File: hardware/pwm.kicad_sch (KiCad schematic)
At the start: 0 parts

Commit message: block refactoring
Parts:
- added D10: D_SCHOTTKY_30V, Diode_SMD:D_SOD-123, symbol Device:D_Schottky
- added J5: Conn_01x02/PWM, TerminalBlock:TerminalBlock_Altech_AK300-2_P5.00mm, symbol Connector_Generic:Conn_01x02
- added JP1: SolderJumper_3_Bridged12, Jumper:SolderJumper-3_P1.3mm_Bridged12_Pad1.0x1.5mm_NumberLabels, symbol Jumper:SolderJumper_3_Bridged12
- added Q2: AO3400A, Package_TO_SOT_SMD:SOT-23, symbol Transistor_FET:AO3400A
- added R7: 10k, Resistor_SMD:R_0603_1608Metric, symbol Device:R
- added R8: 100, Resistor_SMD:R_0603_1608Metric, symbol Device:R
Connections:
- new net: Q2.1 (G), R8.2
- new net +5V: JP1.1 (A)
- new net GND: Q2.2 (S), R7.1
- new net PWM1: R7.2, R8.1
- new net PWM_NEG: D10.2 (A), J5.1 (Pin_1), Q2.3 (D)
- new net PWM_POS: D10.1 (K), J5.2 (Pin_2), JP1.2 (C)
- new net VIN_PROTECTED: JP1.3 (B)

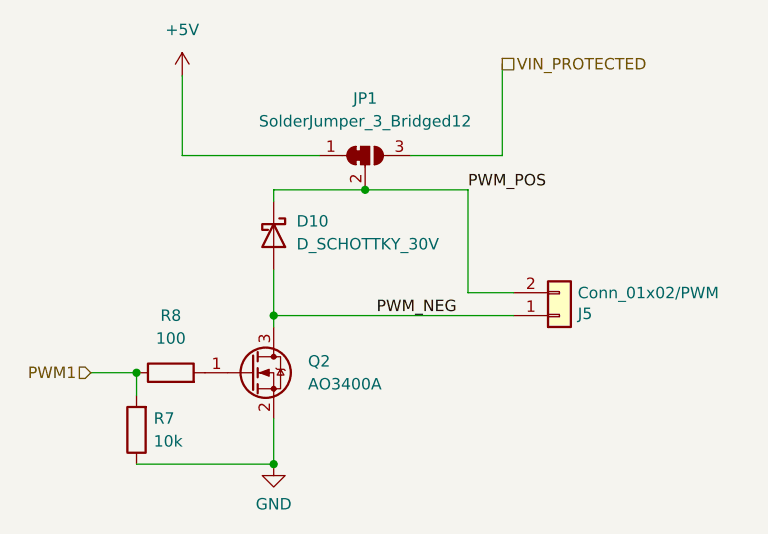
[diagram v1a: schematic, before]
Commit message: Added 3D models and ran freerouting
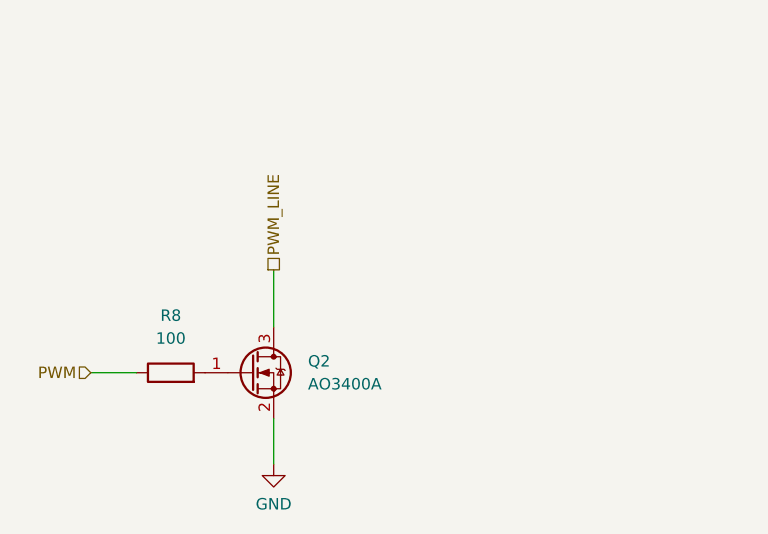
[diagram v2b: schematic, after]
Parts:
- removed D10: D_SCHOTTKY_30V, Diode_SMD:D_SOD-123, symbol Device:D_Schottky
- removed J5: Conn_01x02/PWM, TerminalBlock:TerminalBlock_Altech_AK300-2_P5.00mm, symbol Connector_Generic:Conn_01x02
- removed JP1: SolderJumper_3_Bridged12, Jumper:SolderJumper-3_P1.3mm_Bridged12_Pad1.0x1.5mm_NumberLabels, symbol Jumper:SolderJumper_3_Bridged12
- removed R7: 10k, Resistor_SMD:R_0603_1608Metric, symbol Device:R
- R8: footprint Resistor_SMD:R_0603_1608Metric -> Resistor_SMD:R_0805_2012Metric
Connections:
- net PWM1 renamed PWM
- net PWM_NEG renamed PWM_LINE
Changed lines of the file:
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@@
 (kicad_sch (version 20230121) (generator eeschema)
   (paper "A4")
-  (junction (at 191.77 62.23) (diameter 0) (color 0 0 0 0)
-  )
-  (junction (at 181.61 92.71) (diameter 0) (color 0 0 0 0)
-  )
-  (junction (at 181.61 76.2) (diameter 0) (color 0 0 0 0)
-  )
-  (junction (at 166.37 82.55) (diameter 0) (color 0 0 0 0)
-  )
-  (wire (pts (xy 203.2 73.66) (xy 208.28 73.66))
-    (stroke (width 0) (type default))
-  )
-  (wire (pts (xy 166.37 82.55) (xy 166.37 85.09))
-    (stroke (width 0) (type default))
-  )
-  (wire (pts (xy 181.61 62.23) (xy 181.61 63.5))
-    (stroke (width 0) (type default))
-  )
   (wire (pts (xy 181.61 87.63) (xy 181.61 92.71))
-    (stroke (width 0) (type default))
-  )
-  (wire (pts (xy 181.61 62.23) (xy 191.77 62.23))
-    (stroke (width 0) (type default))
-  )
-  (wire (pts (xy 171.45 49.53) (xy 171.45 58.42))
-    (stroke (width 0) (type default))
-  )
-  (wire (pts (xy 181.61 76.2) (xy 208.28 76.2))
-    (stroke (width 0) (type default))
-  )
-  (wire (pts (xy 191.77 62.23) (xy 203.2 62.23))
     (stroke (width 0) (type default))
   )
@@
     (stroke (width 0) (type default))
   )
-  (wire (pts (xy 181.61 76.2) (xy 181.61 77.47))
+  (wire (pts (xy 181.61 71.12) (xy 181.61 77.47))
     (stroke (width 0) (type default))
   )
-  (wire (pts (xy 166.37 92.71) (xy 181.61 92.71))
-    (stroke (width 0) (type default))
-  )
-  (wire (pts (xy 207.01 58.42) (xy 196.85 58.42))
-    (stroke (width 0) (type default))
-  )
-  (wire (pts (xy 181.61 71.12) (xy 181.61 76.2))
-    (stroke (width 0) (type default))
-  )
-  (wire (pts (xy 171.45 58.42) (xy 186.69 58.42))
-    (stroke (width 0) (type default))
-  )
-  (wire (pts (xy 207.01 48.26) (xy 207.01 58.42))
-    (stroke (width 0) (type default))
-  )
-  (wire (pts (xy 203.2 62.23) (xy 203.2 73.66))
-    (stroke (width 0) (type default))
-  )
-  (label "PWM_NEG" (at 193.04 76.2 0) (fields_autoplaced)
-    (effects (font (size 1.27 1.27)) (justify left bottom))
-  )
-  (label "PWM_POS" (at 203.2 62.23 0) (fields_autoplaced)
-    (effects (font (size 1.27 1.27)) (justify left bottom))
-  )
-  (hierarchical_label "VIN_PROTECTED" (shape passive) (at 207.01 48.26 0) (fields_autoplaced)
-    (effects (font (size 1.27 1.27)) (justify left))
-  )
-  (hierarchical_label "PWM1" (shape input) (at 161.29 82.55 180) (fields_autoplaced)
+  (hierarchical_label "PWM" (shape input) (at 161.29 82.55 180) (fields_autoplaced)
     (effects (font (size 1.27 1.27)) (justify right))
   )
-  (symbol (lib_id "Device:D_Schottky") (at 181.61 67.31 270) (unit 1)
-    (in_bom yes) (on_board yes) (dnp no) (fields_autoplaced)
-    (property "Reference" "D10" (at 184.15 65.7225 90)
-      (effects (font (size 1.27 1.27)) (justify left))
-    )
-    (property "Value" "D_SCHOTTKY_30V" (at 184.15 68.2625 90)
-      (effects (font (size 1.27 1.27)) (justify left))
-    )
-    (property "Footprint" "Diode_SMD:D_SOD-123" (at 181.61 67.31 0)
-      (effects (font (size 1.27 1.27)) hide)
-    )
-    (property "Datasheet" "~" (at 181.61 67.31 0)
-      (effects (font (size 1.27 1.27)) hide)
-    )
-    (property "Cost" "0.0297" (at 181.61 67.31 0)
-      (effects (font (size 1.27 1.27)) hide)
-    )
-    (property "LCSC" "C8598" (at 181.61 67.31 0)
-      (effects (font (size 1.27 1.27)) hide)
-    )
-    (property "Part" "B5819W SL" (at 181.61 67.31 0)
-      (effects (font (size 1.27 1.27)) hide)
-    )
-    (pin "1")
-    (pin "2")
-    (instances
-      (project "esp32-multitool"
-        (path "/3d8a08e7-1222-4d27-bd08-b4e997cf9472/091011c6-be4e-4c21-96a3-2250503f4bfb"
-          (reference "D10") (unit 1)
-        )
-      )
-    )
+  (hierarchical_label "PWM_LINE" (shape passive) (at 181.61 71.12 90) (fields_autoplaced)
+    (effects (font (size 1.27 1.27)) (justify left))
   )
   (symbol (lib_id "Transistor_FET:AO3400A") (at 179.07 82.55 0) (unit 1)
@@
           (reference "Q2") (unit 1)
         )
-      )
-    )
-  )
-  (symbol (lib_id "power:+5V") (at 171.45 49.53 0) (unit 1)
-    (in_bom yes) (on_board yes) (dnp no) (fields_autoplaced)
-    (property "Reference" "#PWR01" (at 171.45 53.34 0)
-      (effects (font (size 1.27 1.27)) hide)
-    )
-    (property "Value" "+5V" (at 171.45 44.45 0)
-      (effects (font (size 1.27 1.27)))
-    )
-    (property "Footprint" "" (at 171.45 49.53 0)
-      (effects (font (size 1.27 1.27)) hide)
-    )
-    (property "Datasheet" "" (at 171.45 49.53 0)
-      (effects (font (size 1.27 1.27)) hide)
-    )
-    (pin "1")
-    (instances
-      (project "esp32-multitool"
-        (path "/3d8a08e7-1222-4d27-bd08-b4e997cf9472/091011c6-be4e-4c21-96a3-2250503f4bfb"
-          (reference "#PWR01") (unit 1)
-        )
-      )
-    )
-  )
-  (symbol (lib_id "Connector_Generic:Conn_01x02") (at 213.36 76.2 0) (mirror x) (unit 1)
-    (in_bom yes) (on_board yes) (dnp no)
-    (property "Reference" "J5" (at 215.392 75.9968 0)
-      (effects (font (size 1.27 1.27)) (justify left))
-    )
-    (property "Value" "Conn_01x02/PWM" (at 215.392 73.6854 0)
-      (effects (font (size 1.27 1.27)) (justify left))
-    )
-    (property "Footprint" "TerminalBlock:TerminalBlock_Altech_AK300-2_P5.00mm" (at 213.36 76.2 0)
-      (effects (font (size 1.27 1.27)) hide)
-    )
-    (property "Datasheet" "~" (at 213.36 76.2 0)
-      (effects (font (size 1.27 1.27)) hide)
-    )
-    (property "LCSC" "C145961" (at 213.36 76.2 0)
-      (effects (font (size 1.27 1.27)) hide)
-    )
-    (property "Cost" "0.0552" (at 213.36 76.2 0)
-      (effects (font (size 1.27 1.27)) hide)
-    )
-    (property "Part" "C145961" (at 213.36 76.2 0)
-      (effects (font (size 1.27 1.27)) hide)
-    )
-    (pin "1")
-    (pin "2")
-    (instances
-      (project "i2c"
-        (path "/2404772b-3ee1-43f3-b842-72bbeb108397"
-          (reference "J5") (unit 1)
-        )
-      )
-      (project "esp32-multitool"
-        (path "/3d8a08e7-1222-4d27-bd08-b4e997cf9472/f9d349b3-837f-44a8-8ae1-0f3a2a1be1fb"
-          (reference "J3") (unit 1)
-        )
-        (path "/3d8a08e7-1222-4d27-bd08-b4e997cf9472/091011c6-be4e-4c21-96a3-2250503f4bfb"
-          (reference "J8") (unit 1)
+        (path "/3d8a08e7-1222-4d27-bd08-b4e997cf9472/7d31a057-7aa5-446b-bc15-c25b1994b237"
+          (reference "Q1") (unit 1)
         )
       )
@@
           (reference "#PWR029") (unit 1)
         )
-      )
-    )
-  )
-  (symbol (lib_id "Device:R") (at 166.37 88.9 180) (unit 1)
-    (in_bom yes) (on_board yes) (dnp no) (fields_autoplaced)
-    (property "Reference" "R7" (at 168.275 87.6299 0)
-      (effects (font (size 1.27 1.27)) (justify right))
-    )
-    (property "Value" "10k" (at 168.275 90.1699 0)
-      (effects (font (size 1.27 1.27)) (justify right))
-    )
-    (property "Footprint" "Resistor_SMD:R_0603_1608Metric" (at 168.148 88.9 90)
-      (effects (font (size 1.27 1.27)) hide)
-    )
-    (property "Datasheet" "~" (at 166.37 88.9 0)
-      (effects (font (size 1.27 1.27)) hide)
-    )
-    (property "Cost" "0.0005" (at 166.37 88.9 0)
-      (effects (font (size 1.27 1.27)) hide)
-    )
-    (property "LCSC" "0603WAF1002T5E" (at 166.37 88.9 0)
-      (effects (font (size 1.27 1.27)) hide)
-    )
-    (property "Part" "0603WAF1002T5E" (at 166.37 88.9 0)
-      (effects (font (size 1.27 1.27)) hide)
-    )
-    (pin "1")
-    (pin "2")
-    (instances
-      (project "esp32-multitool"
-        (path "/3d8a08e7-1222-4d27-bd08-b4e997cf9472/091011c6-be4e-4c21-96a3-2250503f4bfb"
-          (reference "R7") (unit 1)
+        (path "/3d8a08e7-1222-4d27-bd08-b4e997cf9472/7d31a057-7aa5-446b-bc15-c25b1994b237"
+          (reference "#PWR024") (unit 1)
         )
       )
@@
       (effects (font (size 1.27 1.27)))
     )
-    (property "Footprint" "Resistor_SMD:R_0603_1608Metric" (at 170.18 84.328 90)
+    (property "Footprint" "Resistor_SMD:R_0805_2012Metric" (at 170.18 84.328 90)
       (effects (font (size 1.27 1.27)) hide)
     )
@@
           (reference "R8") (unit 1)
         )
-      )
-    )
-  )
-  (symbol (lib_id "Jumper:SolderJumper_3_Bridged12") (at 191.77 58.42 0) (unit 1)
-    (in_bom yes) (on_board yes) (dnp no) (fields_autoplaced)
-    (property "Reference" "JP1" (at 191.77 52.07 0)
-      (effects (font (size 1.27 1.27)))
-    )
-    (property "Value" "SolderJumper_3_Bridged12" (at 191.77 54.61 0)
-      (effects (font (size 1.27 1.27)))
-    )
-    (property "Footprint" "Jumper:SolderJumper-3_P1.3mm_Bridged12_Pad1.0x1.5mm_NumberLabels" (at 191.77 58.42 0)
-      (effects (font (size 1.27 1.27)) hide)
-    )
-    (property "Datasheet" "~" (at 191.77 58.42 0)
-      (effects (font (size 1.27 1.27)) hide)
-    )
-    (pin "1")
-    (pin "2")
-    (pin "3")
-    (instances
-      (project "esp32-multitool"
-        (path "/3d8a08e7-1222-4d27-bd08-b4e997cf9472/091011c6-be4e-4c21-96a3-2250503f4bfb"
-          (reference "JP1") (unit 1)
+        (path "/3d8a08e7-1222-4d27-bd08-b4e997cf9472/7d31a057-7aa5-446b-bc15-c25b1994b237"
+          (reference "R7") (unit 1)
         )
       )
